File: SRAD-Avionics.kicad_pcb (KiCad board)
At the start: 4 copper layers, 263.5 x 93.9 mm, 17 parts, among them J1 Conn_01x02_Socket, U1 MAX-8C, U2 STM32H503RBTx, U3 MCP73831-2-MC, U4 TC2185-3.3VxCTTR

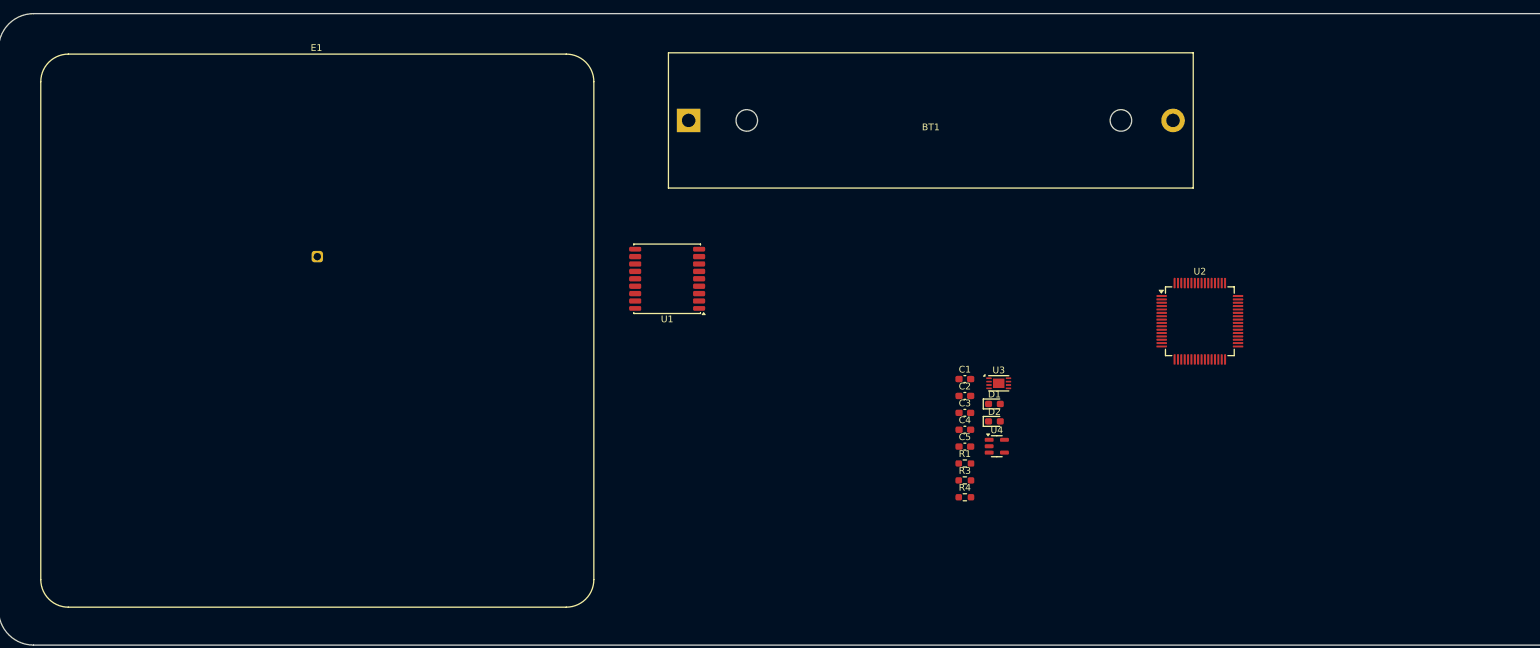
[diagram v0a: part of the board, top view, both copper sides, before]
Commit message: Added USB C and CAN interfaces to schematic
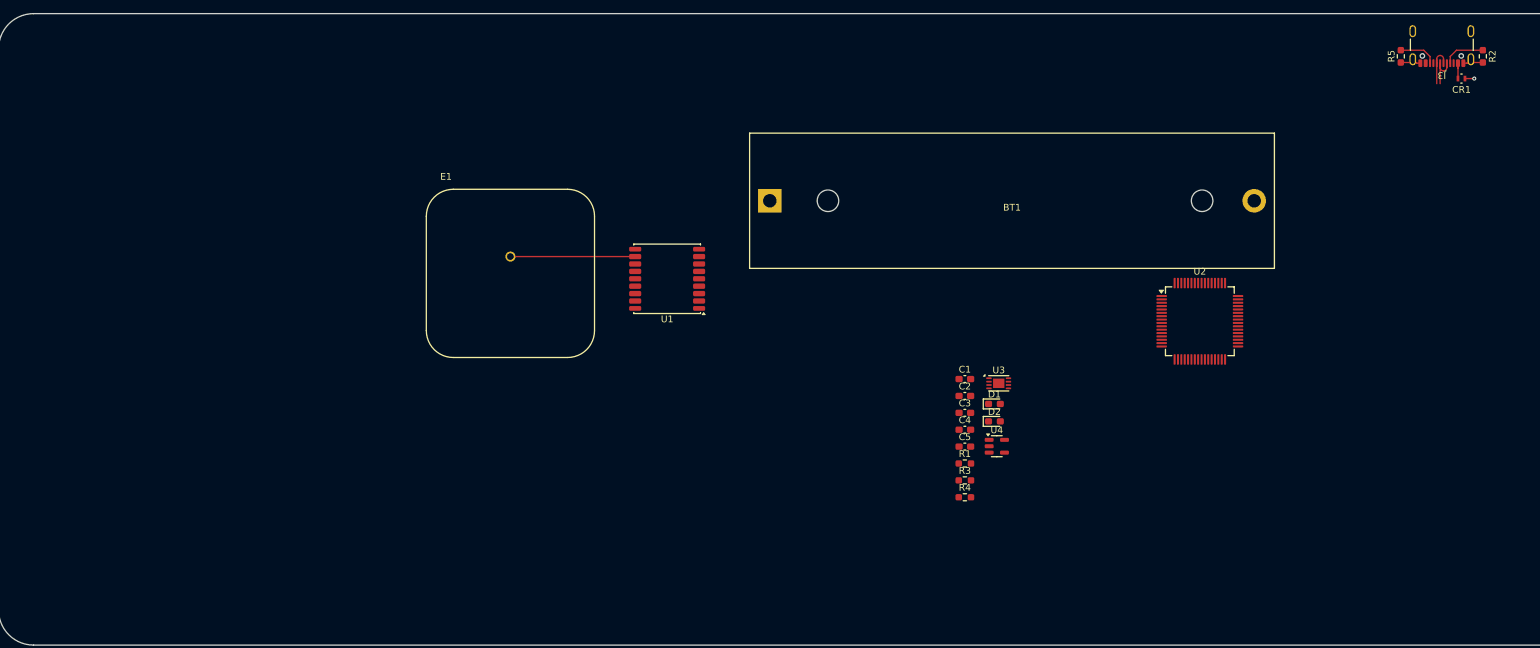
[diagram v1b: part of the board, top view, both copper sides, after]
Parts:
- added CR1: ESDA7P60-1U1M, footprints:ZDO_1610_STM, F.Cu at (233.4, 42.5)
- added J3: USB_C_Receptacle_USB2.0_16P, Connector_USB:USB_C_Receptacle_GCT_USB4105-xx-A_16P_TopMnt_Horizontal, F.Cu at (230.5, 36.6)
- added R2: 5.1k, Resistor_SMD:R_0603_1608Metric_Pad0.98x0.95mm_HandSolder, F.Cu at (236.6, 39.2)
- added R5: 5.1k, Resistor_SMD:R_0603_1608Metric_Pad0.98x0.95mm_HandSolder, F.Cu at (224.4, 39.2)
- E1: value APAE1575R1840AADB7-T -> APAE1590R2540AKDB1-T; footprint RF_Antenna:Abracon_APAES868R8060C16-T -> APAE1590R2540AKDB1_T:XDCR_APAE1590R2540AKDB1-T
- moved E1 28.8 mm to (92.1, 71.5)
- moved BT1 17.0 mm to (130.6, 60.7)
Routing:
- net Net-(U1-RF_IN): track 0.00 -> 18.5 mm
- net GNDD: track 0.00 -> 8.05 mm, vias 0 -> 1
- net Net-(J3-CC1): track 0.00 -> 6.23 mm
- net /USB C Interface/D_N: track 0.00 -> 5.87 mm
- net /USB C Interface/D_P: track 0.00 -> 5.86 mm
- net Net-(J3-CC2): track 0.00 -> 5.72 mm
- net /USB C Interface/V_USB: track 0.00 -> 2.29 mm
- added copper zone on In1.Cu, net GNDD

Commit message: Routed USB interface from port to MCU and CAN interface from connector to transceiver
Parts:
- removed E1: APAE1590R2540AKDB1-T, APAE1590R2540AKDB1_T:XDCR_APAE1590R2540AKDB1-T
- added C10: 100nF, Capacitor_SMD:C_0603_1608Metric_Pad1.08x0.95mm_HandSolder, F.Cu at (177.2, 101.8)
- added C11: 100nF, Capacitor_SMD:C_0603_1608Metric_Pad1.08x0.95mm_HandSolder, F.Cu at (177.2, 104.3)
- added C12: 4.7uF, Capacitor_SMD:C_0603_1608Metric_Pad1.08x0.95mm_HandSolder, F.Cu at (177.2, 106.8)
- added C13: 100nF, Capacitor_SMD:C_0603_1608Metric_Pad1.08x0.95mm_HandSolder, F.Cu at (177.2, 109.3)
- added C14: 1uF, Capacitor_SMD:C_0603_1608Metric_Pad1.08x0.95mm_HandSolder, F.Cu at (177.2, 111.9)
- added C15: 4.7uF, Capacitor_SMD:C_0603_1608Metric_Pad1.08x0.95mm_HandSolder, F.Cu at (162.7, 116.7)
- added C16: 100nF, Capacitor_SMD:C_0603_1608Metric_Pad1.08x0.95mm_HandSolder, F.Cu at (159.1, 106.0)
- added C17: 4.7uF, Capacitor_SMD:C_0603_1608Metric_Pad1.08x0.95mm_HandSolder, F.Cu at (166.2, 106.0)
- added C18: 100nF, Capacitor_SMD:C_0603_1608Metric_Pad1.08x0.95mm_HandSolder, F.Cu at (143.8, 101.9)
- added C19: 10uF, Capacitor_Tantalum_SMD:CP_EIA-3216-18_Kemet-A_Pad1.58x1.35mm_HandSolder, F.Cu at (149.4, 102.1)
- added C20: 100nF, Capacitor_SMD:C_0603_1608Metric_Pad1.08x0.95mm_HandSolder, F.Cu at (143.8, 104.4)
- added C6: 2.2uF, Capacitor_SMD:C_0603_1608Metric_Pad1.08x0.95mm_HandSolder, F.Cu at (177.2, 91.8)
- added C7: 2.2uF, Capacitor_SMD:C_0603_1608Metric_Pad1.08x0.95mm_HandSolder, F.Cu at (177.2, 94.3)
- added C8: 100nF, Capacitor_SMD:C_0603_1608Metric_Pad1.08x0.95mm_HandSolder, F.Cu at (177.2, 96.8)
- added C9: 100nF, Capacitor_SMD:C_0603_1608Metric_Pad1.08x0.95mm_HandSolder, F.Cu at (177.2, 99.3)
- added D3: NUP2105L, Package_TO_SOT_SMD:SOT-23, F.Cu at (162.7, 120.9)
- added J2: Conn_01x02_Socket, TerminalBlock_Phoenix:TerminalBlock_Phoenix_MKDS-1,5-2-5.08_1x02_P5.08mm_Horizontal, F.Cu at (160.0, 129.7)
- added R6: 10k, Resistor_SMD:R_0603_1608Metric_Pad0.98x0.95mm_HandSolder, F.Cu at (148.0, 82.6)
- added R7: 62, Resistor_SMD:R_0805_2012Metric_Pad1.20x1.40mm_HandSolder, F.Cu at (164.6, 116.9)
- added R8: 62, Resistor_SMD:R_0805_2012Metric_Pad1.20x1.40mm_HandSolder, F.Cu at (160.6, 116.9)
- added SW1: SW_DIP_x01, Button_Switch_SMD:SW_DIP_SPSTx01_Slide_Copal_CHS-01B_W7.62mm_P1.27mm, F.Cu at (148.0, 75.8)
- added TP1: TestPoint, TestPoint:TestPoint_Loop_D2.60mm_Drill1.6mm_Beaded, F.Cu at (181.9, 93.0)
- added TP2: TestPoint, TestPoint:TestPoint_Loop_D2.60mm_Drill1.6mm_Beaded, F.Cu at (181.9, 98.1)
- added TP3: TestPoint, TestPoint:TestPoint_Loop_D2.60mm_Drill1.6mm_Beaded, F.Cu at (181.9, 103.1)
- added TP4: TestPoint, TestPoint:TestPoint_Loop_D2.60mm_Drill1.6mm_Beaded, F.Cu at (148.1, 58.6)
- added U5: USBLC6-2SC6, Package_TO_SOT_SMD:SOT-23-6, F.Cu at (160.2, 66.3)
- added U6: TCAN332G, Package_SO:SOIC-8_3.9x4.9mm_P1.27mm, F.Cu at (162.7, 107.8)
- added U7: ADXL375BCCZ, Package_LGA:LGA-14_3x5mm_P0.8mm_LayoutBorder1x6y, F.Cu at (148.7, 97.2)
- BT1: value BH-18650-PC -> Battery_Cell
- U1: value MAX-8C -> MS5607-02BA; footprint RF_GPS:ublox_MAX -> Package_LGA:LGA-8_3x5mm_P1.25mm
- moved J1 129.7 mm to (141.8, 129.7), turned to 0 degrees
- moved R2 72.9 mm to (166.8, 60.3)
- moved J3 72.9 mm to (160.7, 57.6)
- moved R5 72.9 mm to (154.6, 60.3)
- moved CR1 72.8 mm to (163.6, 63.2)
- moved U4 40.2 mm to (174.8, 58.4)
- moved U3 39.2 mm to (137.7, 59.3)
- moved U1 38.1 mm to (144.1, 97.4), turned to 0 degrees
- moved U2 32.3 mm to (162.2, 78.2), turned to 90 degrees
- moved C1 27.1 mm to (175.5, 65.3)
- moved C2 27.1 mm to (175.5, 67.8)
- moved C4 27.1 mm to (175.5, 72.8)
- moved C5 27.1 mm to (175.5, 75.3)
- moved D1 27.1 mm to (179.9, 69.0)
- moved D2 27.1 mm to (179.9, 71.5)
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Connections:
- net /USB C Interface/D_N renamed Net-(J3-D--PadA7)
- net /USB C Interface/D_P renamed Net-(J3-D+-PadA6)
- BT1 pad 1: (no net) -> /Battery Management/V_BAT
- BT1 pad 2: (no net) -> GNDD
- CR1 pad 1: /USB C Interface/V_USB -> /Battery Management/V_USB
- J3 pad A4: /USB C Interface/V_USB -> /Battery Management/V_USB
- J3 pad A9: /USB C Interface/V_USB -> /Battery Management/V_USB
- J3 pad B4: /USB C Interface/V_USB -> /Battery Management/V_USB
- J3 pad B9: /USB C Interface/V_USB -> /Battery Management/V_USB
- U1 pad 2: /GPS_TX -> GNDD
- U1 pad 3: /GPS_RX -> GNDD
- U1 pad 4: unconnected-(U1-TIMEPULSE-Pad4) -> /Sensors/pres_cs
- U1 pad 5: unconnected-(U1-EXTINT-Pad5) -> /Sensors/pres_cs
- U1 pad 6: unconnected-(U1-V_BCKP-Pad6) -> /Sensors/pres_miso
- U1 pad 7: GNDD -> /Sensors/pres_mosi
- U1 pad 8: GNDD -> /Sensors/pres_sclk
- U2 pad 1: unconnected-(U2-VBAT-Pad1) -> +3.3V
- U2 pad 12: unconnected-(U2-VSSA-Pad12) -> GNDA
- U2 pad 13: unconnected-(U2-VDDA-Pad13) -> VDDA
- U2 pad 18: Net-(U2-VSS-Pad18) -> GNDD
- U2 pad 30: unconnected-(U2-VCAP-Pad30) -> Net-(C6-Pad1)
- U2 pad 31: Net-(U2-VSS-Pad18) -> GNDD
- U2 pad 44: unconnected-(U2-PA11-Pad44) -> /USB_D_N
- U2 pad 45: unconnected-(U2-PA12-Pad45) -> /USB_D_P
- U2 pad 47: Net-(U2-VSS-Pad18) -> GNDD
- U2 pad 59: unconnected-(U2-PB7-Pad59) -> /FDCAN_TX
- U2 pad 60: unconnected-(U2-BOOT0-Pad60) -> /BOOT0
- U2 pad 61: unconnected-(U2-PB8-Pad61) -> /FDCAN_RX
- U2 pad 62: unconnected-(U2-VCAP-Pad62) -> Net-(C6-Pad1)
- U2 pad 63: Net-(U2-VSS-Pad18) -> GNDD
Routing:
- net /CAN Interface/CAN_L: track 0.00 -> 22.5 mm
- net /CAN Interface/CAN_H: track 0.00 -> 22.4 mm
- net Net-(U1-RF_IN): track 18.5 -> 0.00 mm
- net +3.3V: track 0.00 -> 17.0 mm, vias 0 -> 6
- net GNDD: track 8.05 -> 22.4 mm, vias 1 -> 12
- net /USB_D_P: track 0.00 -> 5.94 mm
- net /USB_D_N: track 0.00 -> 5.93 mm
- net /Battery Management/V_USB: track 0.00 -> 5.80 mm, vias 0 -> 3
- net Net-(C15-Pad1): track 0.00 -> 3.94 mm
- net /USB C Interface/V_USB: track 2.29 -> 0.00 mm
- net /BOOT0: track 0.00 -> 2.14 mm
- net Net-(J3-D--PadA7): track 5.87 -> 7.91 mm
- net Net-(J3-D+-PadA6): track 5.86 -> 7.51 mm
- added copper zone on In2.Cu, net /Battery Management/V_USB
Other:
- board size 263.5 x 93.9 mm -> 75.8 x 82.9 mm
- board text added: "${REFERENCE}"
- board text added: "PCB Edge"
